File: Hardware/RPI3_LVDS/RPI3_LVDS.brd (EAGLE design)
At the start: 53.2 x 63.1 mm, 37 parts, among them J2 87832-6422, J3 1775470-6, U1 DS90C365A, U2 LM1085ISX-5.0/NOPB, U3 ADP3338AKCZ-3.3-RL

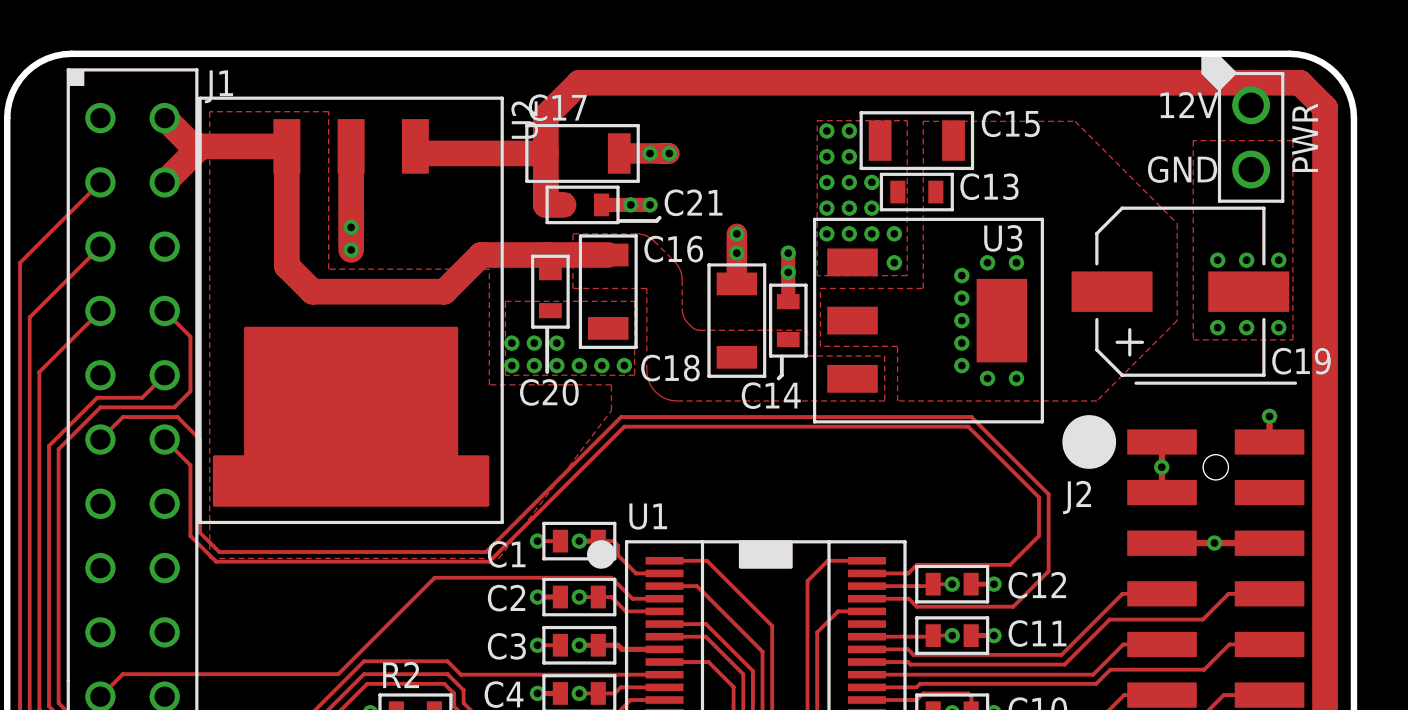
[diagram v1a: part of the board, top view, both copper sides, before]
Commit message: Fixed LM1085
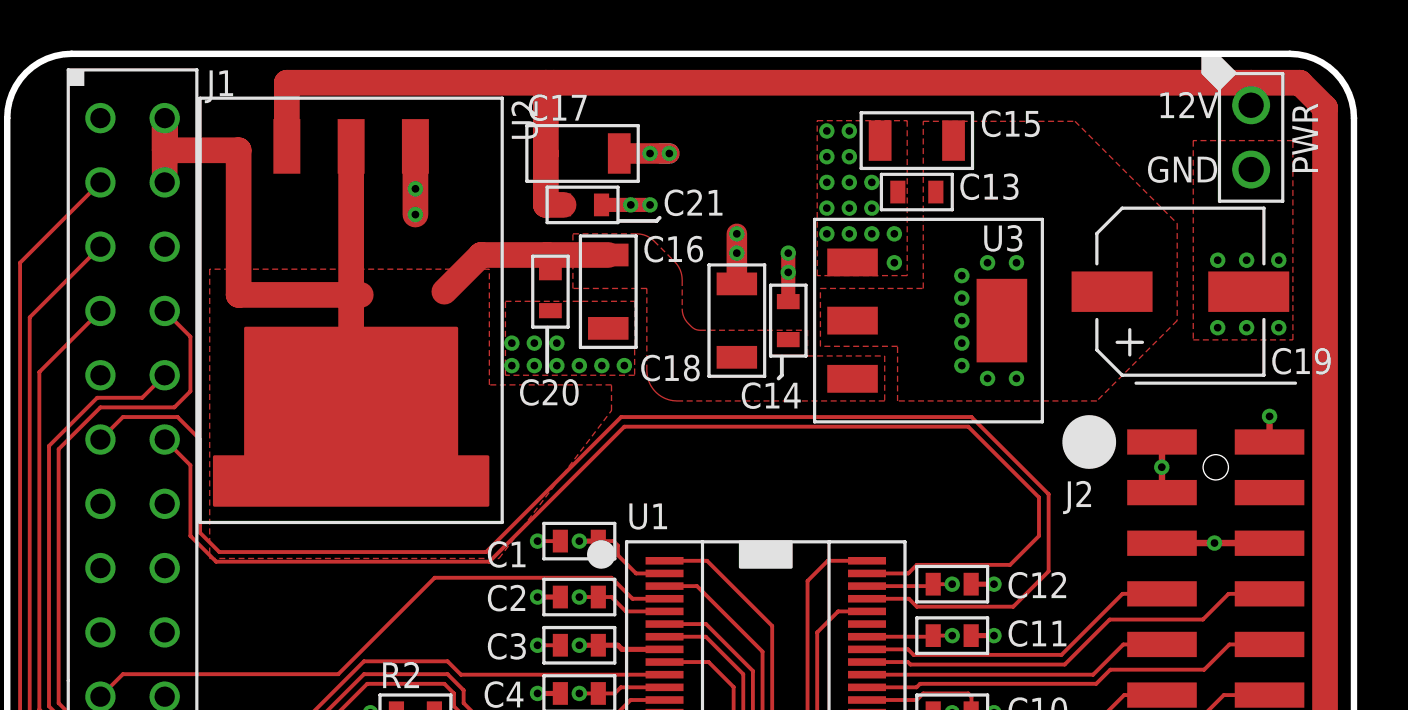
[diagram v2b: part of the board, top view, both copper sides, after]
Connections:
- net 12.0V: now also U2.P$3; no longer U2.P$1
- net 5.0V: now also U2.P$2; no longer U2.P$3
- net GND: now also U2.P$1; no longer U2.P$2
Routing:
- net 12.0V: track 118.8 -> 127.0 mm
- net 5.0V: track 26.5 -> 34.0 mm
- net GND: track 86.0 -> 84.6 mm
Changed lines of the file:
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@@
 <setting verticaltext="up"/>
 </settings>
-<grid distance="100" unitdist="mil" unit="mil" style="lines" multiple="1" display="no" altdistance="1" altunitdist="mil" altunit="mil"/>
+<grid distance="10" unitdist="mil" unit="mil" style="lines" multiple="1" display="no" altdistance="1" altunitdist="mil" altunit="mil"/>
 <layers>
 <layer number="1" name="Top" color="4" fill="1" visible="yes" active="yes"/>
@@
 <element name="U$14" library="PP_Aesthetics" package="LHE_FRAME" value="LHE_FRAME" x="45.974" y="56.515" rot="MR0">
 <attribute name="DNAME" value="Parker Dillmann" x="45.974" y="56.515" size="1.778" layer="28" rot="MR0" display="off"/>
-<attribute name="REVNUM" value="REV: 2" x="45.974" y="56.515" size="1.778" layer="28" rot="MR0" display="off"/>
+<attribute name="REVNUM" value="REV: 3" x="45.974" y="56.515" size="1.778" layer="28" rot="MR0" display="off"/>
 </element>
 <element name="LOGO1" library="PP_Aesthetics" package="SPOOKY_LOGO" value="SPOOKY_LOGOSPOOKY_LOGO" x="42.672" y="3.175" rot="R90"/>
@@
 <vertex x="53.213" y="2.54" curve="-90"/>
 </polygon>
-<contactref element="U2" pad="P$2"/>
-<wire x1="13.589" y1="59.4614" x2="13.589" y2="55.372" width="1.016" layer="1"/>
-<via x="13.589" y="55.372" extent="1-16" drill="0.3048"/>
-<via x="13.589" y="56.261" extent="1-16" drill="0.3048"/>
+<contactref element="U2" pad="P$1"/>
+<via x="16.129" y="56.769" extent="1-16" drill="0.3048"/>
+<via x="16.129" y="57.785" extent="1-16" drill="0.3048"/>
+<wire x1="16.129" y1="59.4614" x2="16.129" y2="56.769" width="1.016" layer="1"/>
 </signal>
 <signal name="ODD0-">
@@
 <vertex x="22.352" y="53.848"/>
 </polygon>
-<contactref element="U2" pad="P$3"/>
-<wire x1="11.049" y1="59.4614" x2="7.6454" y2="59.4614" width="1.016" layer="1"/>
-<wire x1="7.6454" y1="59.4614" x2="7.3406" y2="59.4614" width="1.016" layer="1"/>
-<wire x1="7.3406" y1="59.4614" x2="6.223" y2="60.579" width="1.016" layer="1"/>
-<wire x1="6.223" y1="58.039" x2="7.6454" y2="59.4614" width="1.016" layer="1"/>
-<wire x1="11.049" y1="59.4614" x2="11.049" y2="54.737" width="1.016" layer="1"/>
-<wire x1="11.049" y1="54.737" x2="12.065" y2="53.721" width="1.016" layer="1"/>
-<wire x1="12.065" y1="53.721" x2="17.272" y2="53.721" width="1.016" layer="1"/>
+<contactref element="U2" pad="P$2"/>
 <wire x1="17.272" y1="53.721" x2="18.722" y2="55.171" width="1.016" layer="1"/>
 <wire x1="18.722" y1="55.171" x2="21.336" y2="55.171" width="1.016" layer="1"/>
@@
 <vertex x="19.05" y="50.038"/>
 <vertex x="19.05" y="54.61"/>
-<vertex x="12.7" y="54.61"/>
-<vertex x="12.7" y="60.833"/>
-<vertex x="8.001" y="60.833"/>
+<vertex x="8.001" y="54.61"/>
 </polygon>
+<wire x1="13.589" y1="59.4614" x2="13.589" y2="53.594" width="1.016" layer="1"/>
+<wire x1="13.589" y1="53.594" x2="13.589" y2="50.5714" width="1.016" layer="1"/>
+<wire x1="6.223" y1="60.579" x2="6.223" y2="58.039" width="1.016" layer="1"/>
+<wire x1="6.223" y1="60.579" x2="6.223" y2="59.309" width="1.016" layer="1"/>
+<wire x1="6.223" y1="59.309" x2="9.144" y2="59.309" width="1.016" layer="1"/>
+<wire x1="9.144" y1="59.309" x2="9.144" y2="53.594" width="1.016" layer="1"/>
+<wire x1="9.144" y1="53.594" x2="13.589" y2="53.594" width="1.016" layer="1"/>
+<wire x1="13.589" y1="53.594" x2="13.97" y2="53.594" width="1.016" layer="1"/>
 </signal>
 <signal name="12.0V">
@@
 <contactref element="C21" pad="P$1"/>
 <contactref element="C17" pad="P$1"/>
-<wire x1="49.149" y1="61.976" x2="22.606" y2="61.976" width="1.016" layer="1"/>
-<wire x1="22.606" y1="61.976" x2="21.283" y2="60.653" width="1.016" layer="1"/>
-<wire x1="21.283" y1="60.653" x2="21.283" y2="59.182" width="1.016" layer="1"/>
+<wire x1="49.149" y1="61.976" x2="21.59" y2="61.976" width="1.016" layer="1"/>
+<wire x1="21.283" y1="61.976" x2="11.049" y2="61.976" width="1.016" layer="1"/>
+<wire x1="21.283" y1="61.976" x2="21.283" y2="59.182" width="1.016" layer="1"/>
 <wire x1="21.283" y1="59.182" x2="21.283" y2="57.15" width="1.016" layer="1"/>
 <wire x1="21.283" y1="57.15" x2="21.983" y2="57.15" width="1.016" layer="1"/>
@@
 <wire x1="51.0781" y1="61.976" x2="49.149" y2="61.976" width="1.016" layer="1"/>
 <wire x1="46.482" y1="5.763" x2="52.07" y2="5.763" width="1.016" layer="1"/>
-<contactref element="U2" pad="P$1"/>
-<wire x1="21.283" y1="59.182" x2="16.4084" y2="59.182" width="1.016" layer="1"/>
-<wire x1="16.4084" y1="59.182" x2="16.129" y2="59.4614" width="1.016" layer="1"/>
+<contactref element="U2" pad="P$3"/>
+<wire x1="11.049" y1="59.4614" x2="11.049" y2="61.976" width="1.016" layer="1"/>
+<wire x1="21.283" y1="61.976" x2="21.59" y2="61.976" width="1.016" layer="1"/>
 </signal>
 </signals>
